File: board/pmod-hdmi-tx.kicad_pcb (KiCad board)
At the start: 2 copper layers, 42 x 43.2 mm, 35 parts, among them P1 PMOD-Device-x2-Type-XHS-Alt, U31 XC9140, U32 REG710-DBV

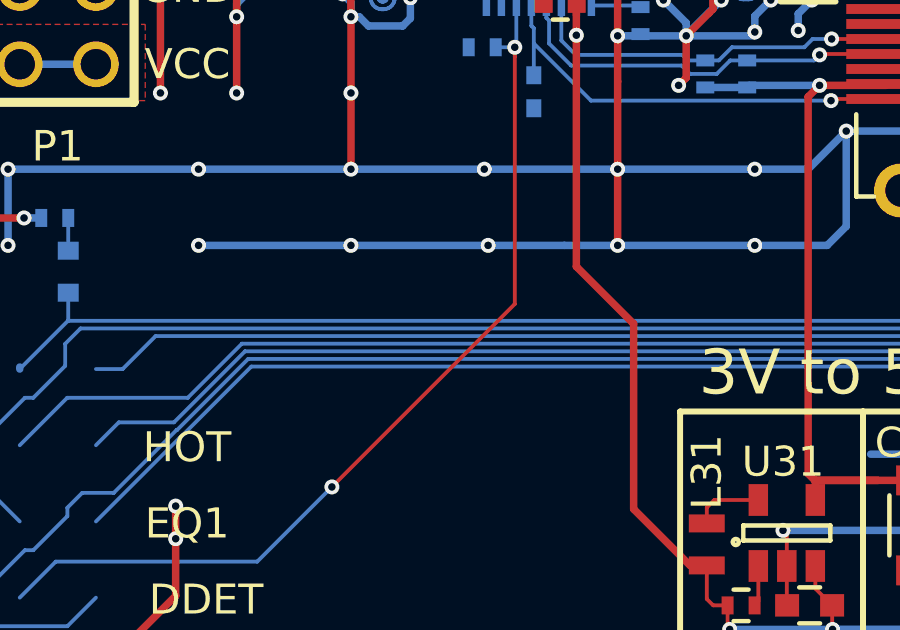
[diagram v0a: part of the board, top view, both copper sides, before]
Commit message: Fiddling with the silkscreen.
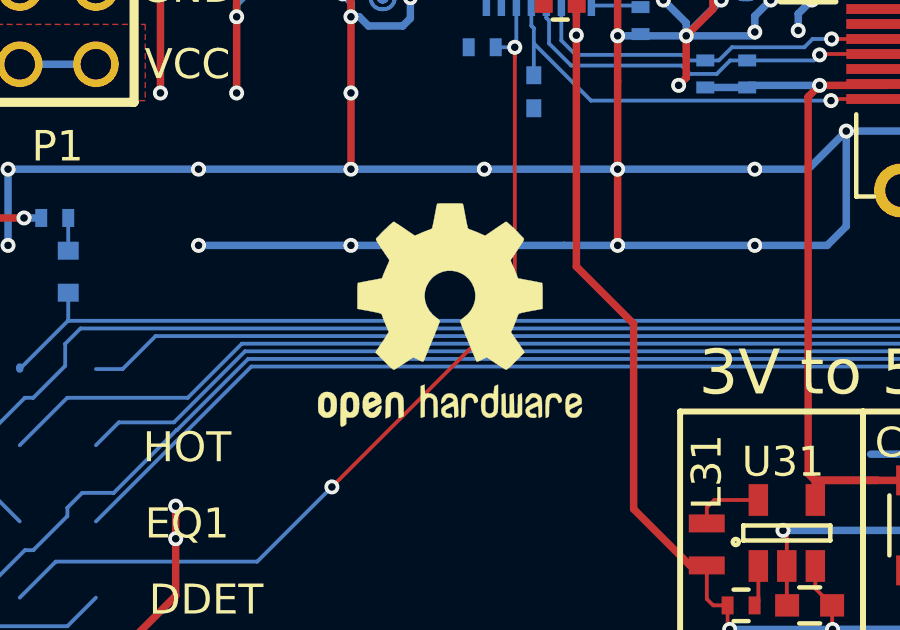
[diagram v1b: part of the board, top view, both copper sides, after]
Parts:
- added REF***: OSHW-Logo2_9.8x8mm_SilkScreen, Symbols:OSHW-Logo2_9.8x8mm_SilkScreen, F.Cu at (98.6, 95.0)
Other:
- board text added: "pmod-hdmi-tx ptn3363"
- board text added: "v0.0"

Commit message: Tweaking embedded version.
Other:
- board text added: "$Id$"
- board text added: "tx0.0"
- board text removed: "v0.0"
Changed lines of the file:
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@@
 (kicad_pcb (version 4) (host pcbnew 4.0.4+e1-6308~48~ubuntu14.04.1-stable)
   (general
-    (links 0)
+    (links 102)
     (no_connects 0)
     (area 48.857144 45.285715 236.214292 120.05)
     (thickness 1.6)
-    (drawings 128)
+    (drawings 129)
     (tracks 1763)
     (zones 0)
@@
       (xy -0.017575 -3.712307) (xy 0 -3.712308) (xy 0.139878 -3.712224)) (layer F.SilkS) (width 0.01))
   )
-  (gr_text v0.0 (at 121.0818 105.156) (layer B.SilkS)
+  (gr_text $Id$ (at 121.1072 109.2454) (layer B.SilkS)
     (effects (font (size 2.159 2.159) (thickness 0.53975)) (justify left mirror))
   )
+  (gr_text tx0.0 (at 121.0818 105.156) (layer B.SilkS)
+    (effects (font (size 2.159 2.159) (thickness 0.53975)) (justify left mirror))
+  )

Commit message: Tweaking a track.
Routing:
- net VCC3V3: track 106.6 -> 107.2 mm
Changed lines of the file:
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@@
     (thickness 1.6)
     (drawings 129)
-    (tracks 1763)
+    (tracks 1764)
     (zones 0)
     (modules 37)
@@
   (via (at 103.8352 75.0062) (size 0.5) (drill 0.25) (layers F.Cu B.Cu) (net 0))
   (via (at 103.8352 79.9846) (size 0.5) (drill 0.25) (layers F.Cu B.Cu) (net 0))
+  (segment (start 107.315 109.22) (end 106.6546 108.5596) (width 0.25) (layer F.Cu) (net 1))
+  (segment (start 106.6546 108.5596) (end 87.7224 108.5596) (width 0.25) (layer F.Cu) (net 1))
+  (segment (start 87.7224 108.5596) (end 86.75 109.532) (width 0.25) (layer F.Cu) (net 1))
   (segment (start 99.187 79.883) (end 99.187 79.502) (width 0.25) (layer F.Cu) (net 1))
   (segment (start 99.187 79.502) (end 98.7044 79.0194) (width 0.25) (layer F.Cu) (net 1))
@@
   (segment (start 104.6734 101.4984) (end 104.6734 95.3262) (width 0.25) (layer F.Cu) (net 1))
   (segment (start 107.1118 103.37864) (end 106.55364 103.37864) (width 0.25) (layer F.Cu) (net 1))
-  (segment (start 107.315 109.22) (end 87.062 109.22) (width 0.25) (layer F.Cu) (net 1))
-  (segment (start 87.062 109.22) (end 86.75 109.532) (width 0.25) (layer F.Cu) (net 1))
   (segment (start 110.49 109.22) (end 107.315 109.22) (width 0.25) (layer F.Cu) (net 1))
   (segment (start 111.3028 108.4072) (end 110.49 109.22) (width 0.25) (layer F.Cu) (net 1))

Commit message: Adding GND/VCC open area.
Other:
- board text added: "647f4a6"
- board text added: "VCC3V3"
- board text added: "tx0.1"
- board text removed: "$Id$"
- board text removed: "tx0.0"
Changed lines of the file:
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@@
-(kicad_pcb (version 4) (host pcbnew 4.0.4+e1-6308~48~ubuntu14.04.1-stable)
+(kicad_pcb (version 4) (host pcbnew 4.0.6-e0-6349~53~ubuntu14.04.1)
   (general
     (links 102)
@@
     (area 48.857144 45.285715 236.214292 120.05)
     (thickness 1.6)
-    (drawings 129)
+    (drawings 131)
     (tracks 1764)
     (zones 0)
@@
     (36 B.SilkS user)
     (37 F.SilkS user)
-    (38 B.Mask user hide)
-    (39 F.Mask user hide)
-    (40 Dwgs.User user hide)
+    (38 B.Mask user)
+    (39 F.Mask user)
+    (40 Dwgs.User user)
     (41 Cmts.User user hide)
     (42 Eco1.User user hide)
@@
       (xy -0.017575 -3.712307) (xy 0 -3.712308) (xy 0.139878 -3.712224)) (layer F.SilkS) (width 0.01))
   )
-  (gr_text $Id$ (at 121.1072 109.2454) (layer B.SilkS)
+  (gr_text GND (at 100.3935 107.6325) (layer B.SilkS)
+    (effects (font (size 1.5 1.5) (thickness 0.3)) (justify mirror))
+  )
+  (gr_text VCC3V3 (at 96.8375 107.7595) (layer F.SilkS)
+    (effects (font (size 1.5 1.5) (thickness 0.3)))
+  )
+  (gr_text 647f4a6 (at 121.1072 109.2454) (layer B.SilkS)
     (effects (font (size 2.159 2.159) (thickness 0.53975)) (justify left mirror))
   )
-  (gr_text tx0.0 (at 121.0818 105.156) (layer B.SilkS)
+  (gr_text tx0.1 (at 121.0818 105.156) (layer B.SilkS)
     (effects (font (size 2.159 2.159) (thickness 0.53975)) (justify left mirror))
   )
@@
       )
     )
+  )
+  (zone (net 0) (net_name "") (layer F.Mask) (hatch edge 0.508)
+    (connect_pads (clearance 0.2))
+    (min_thickness 0.254)
+    (fill yes (arc_segments 16) (thermal_gap 0.508) (thermal_bridge_width 0.508))
+    (polygon
+      (pts
+        (xy 92.453982 108.7755) (xy 97.279982 108.7755) (xy 97.279982 113.3475) (xy 92.453982 113.3475)
+      )
+    )
+  )
+  (zone (net 0) (net_name "") (layer B.Mask) (hatch edge 0.508)
+    (connect_pads (clearance 0.2))
+    (min_thickness 0.254)
+    (fill yes (arc_segments 16) (thermal_gap 0.508) (thermal_bridge_width 0.508))
+    (polygon
+      (pts
+        (xy 97.8535 108.7755) (xy 102.6795 108.7755) (xy 102.6795 113.3475) (xy 97.8535 113.3475)
+      )
+    )

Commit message: Fiddling with the silkscreen more.
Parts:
- moved REF*** 6.66 mm to (100.2, 101.5)
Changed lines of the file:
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@@
     (descr "QMOD Pin Header 2 x 6 pins")
     (tags CONN)
-    (fp_text reference PTX0 (at -0.762 -8.636) (layer F.SilkS)
+    (fp_text reference PTX0 (at -0.898 8.7685) (layer F.SilkS)
       (effects (font (size 1.016 1.016) (thickness 0.254)))
     )
@@
   )
   (module Symbols:OSHW-Logo2_9.8x8mm_SilkScreen (layer F.Cu)
-    (at 98.552 95.0214)
+    (at 100.203 101.473)
     (descr "Open Source Hardware Symbol")
     (tags "Logo Symbol OSHW")
@@
   (gr_line (start 80 113.342) (end 59 113.342) (layer Eco1.User) (width 0.2))
   (gr_line (start 79.5 70.162) (end 59 70.162) (layer Eco1.User) (width 0.2))
-  (gr_text "Low Speed & Control Signals" (at 97.663 111.887) (layer F.SilkS)
-    (effects (font (size 1.5 1.5) (thickness 0.3)))
-  )
-  (gr_text "High Speed" (at 86.995 71.247) (layer F.SilkS)
-    (effects (font (size 1.5 1.5) (thickness 0.3)))
-  )
+  (gr_text "Low Speed & Control Signals" (at 99.441 94.0435) (layer F.SilkS)
+    (effects (font (size 1.5 1.5) (thickness 0.3)))
+  )
+  (gr_text "High Speed" (at 89.0905 71.501) (layer F.SilkS)
+    (effects (font (size 1.5 1.5) (thickness 0.3)))
+  )

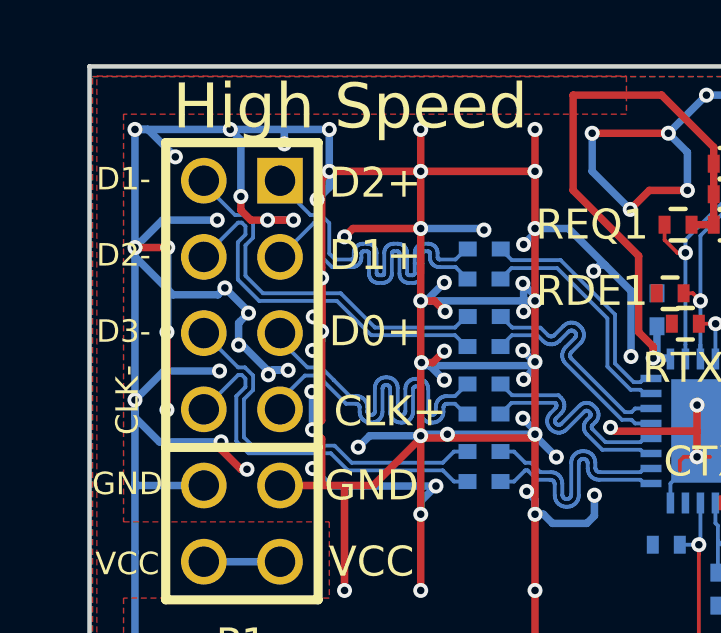
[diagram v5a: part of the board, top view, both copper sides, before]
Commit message: Fixing the high speed labels.
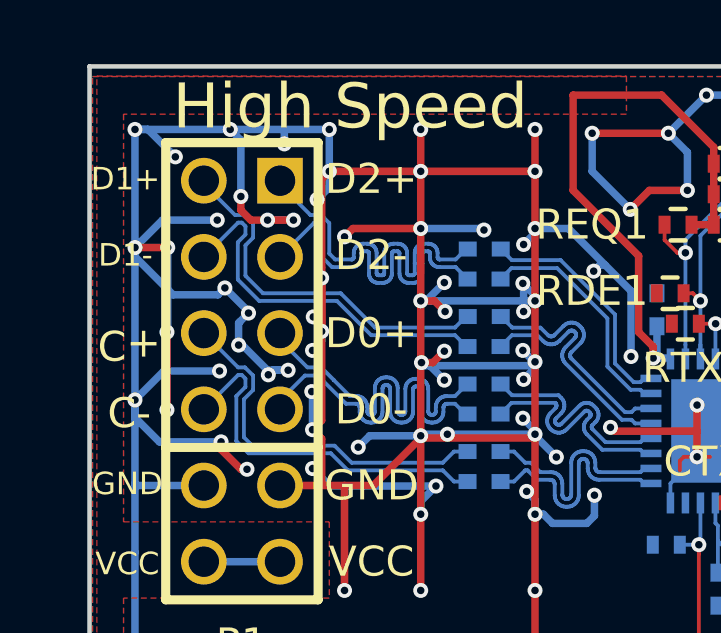
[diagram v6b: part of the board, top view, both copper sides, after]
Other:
- board text added: "C+"
- board text added: "C-"
- board text removed: "CLK+"
- board text removed: "CLK-"
- board text removed: "D3-"
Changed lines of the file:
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@@
   (page A4)
   (layers
-    (0 F.Cu signal)
-    (31 B.Cu signal)
+    (0 F.Cu signal hide)
+    (31 B.Cu signal hide)
     (32 B.Adhes user hide)
     (33 F.Adhes user hide)
@@
     (36 B.SilkS user)
     (37 F.SilkS user)
-    (38 B.Mask user)
-    (39 F.Mask user)
+    (38 B.Mask user hide)
+    (39 F.Mask user hide)
     (40 Dwgs.User user)
     (41 Cmts.User user hide)
@@
       (effects (font (size 1 1) (thickness 0.15)))
     )
-    (fp_text user D2+ (at 4.436 -6.281) (layer F.SilkS)
+    (fp_text user D2+ (at 4.309 -6.408) (layer F.SilkS)
       (effects (font (size 1 1) (thickness 0.15)))
     )
@@
       (xy -0.017575 -3.712307) (xy 0 -3.712308) (xy 0.139878 -3.712224)) (layer F.SilkS) (width 0.01))
   )
+  (gr_text C+ (at 81.7245 79.4385 180) (layer F.SilkS)
+    (effects (font (size 1 1) (thickness 0.15)) (justify mirror))
+  )
   (gr_text GND (at 100.3935 107.6325) (layer B.SilkS)
     (effects (font (size 1.5 1.5) (thickness 0.3)) (justify mirror))
@@
     (effects (font (size 1 1) (thickness 0.15)) (justify mirror))
   )
-  (gr_text CLK- (at 81.153 82.677 90) (layer B.SilkS)
+  (gr_text C- (at 81.7245 81.7245 360) (layer B.SilkS)
     (effects (font (size 1 1) (thickness 0.15)) (justify mirror))
   )
-  (gr_text D0- (at 82.042 79.629 90) (layer B.SilkS)
+  (gr_text C+ (at 81.7245 79.4385 360) (layer B.SilkS)
     (effects (font (size 1 1) (thickness 0.15)) (justify mirror))
   )
@@
     (effects (font (size 1 1) (thickness 0.15)) (justify mirror))
   )
-  (gr_text D2- (at 82.042 74.168 90) (layer B.SilkS)
+  (gr_text D1+ (at 82.042 74.168 90) (layer B.SilkS)
     (effects (font (size 1 1) (thickness 0.15)) (justify mirror))
   )
-  (gr_text CLK+ (at 89.916 81.28) (layer B.SilkS)
+  (gr_text D0- (at 89.789 81.5975) (layer B.SilkS)
     (effects (font (size 1 1) (thickness 0.15)) (justify mirror))
   )
-  (gr_text D0+ (at 89.916 78.74) (layer B.SilkS)
+  (gr_text D0+ (at 89.789 79.0575) (layer B.SilkS)
     (effects (font (size 1 1) (thickness 0.15)) (justify mirror))
   )
-  (gr_text D1+ (at 89.789 76.327) (layer B.SilkS)
+  (gr_text D2- (at 89.789 76.454) (layer B.SilkS)
     (effects (font (size 1 1) (thickness 0.15)) (justify mirror))
   )
@@
     (effects (font (size 0.75 0.75) (thickness 0.15)))
   )
-  (gr_text CLK- (at 81.661 81.28 90) (layer F.SilkS)
+  (gr_text C- (at 81.7245 81.7245 360) (layer F.SilkS)
+    (effects (font (size 1 1) (thickness 0.15)))
+  )
+  (gr_text D1- (at 81.5975 76.454) (layer F.SilkS)
     (effects (font (size 0.75 0.75) (thickness 0.15)))
   )
-  (gr_text D3- (at 81.534 78.994) (layer F.SilkS)
+  (gr_text D1+ (at 81.5975 73.914) (layer F.SilkS)
     (effects (font (size 0.75 0.75) (thickness 0.15)))
   )
-  (gr_text D2- (at 81.534 76.454) (layer F.SilkS)
-    (effects (font (size 0.75 0.75) (thickness 0.15)))
-  )
-  (gr_text D1- (at 81.534 73.914) (layer F.SilkS)
-    (effects (font (size 0.75 0.75) (thickness 0.15)))
-  )
-  (gr_text CLK+ (at 90.424 81.661) (layer F.SilkS)
+  (gr_text D0- (at 89.789 81.5975) (layer F.SilkS)
     (effects (font (size 1 1) (thickness 0.15)))
   )
-  (gr_text D0+ (at 89.916 78.994) (layer F.SilkS)
+  (gr_text D0+ (at 89.789 79.0575) (layer F.SilkS)
     (effects (font (size 1 1) (thickness 0.15)))
   )
-  (gr_text D1+ (at 89.916 76.454) (layer F.SilkS)
+  (gr_text D2- (at 89.789 76.454) (layer F.SilkS)
     (effects (font (size 1 1) (thickness 0.15)))
   )

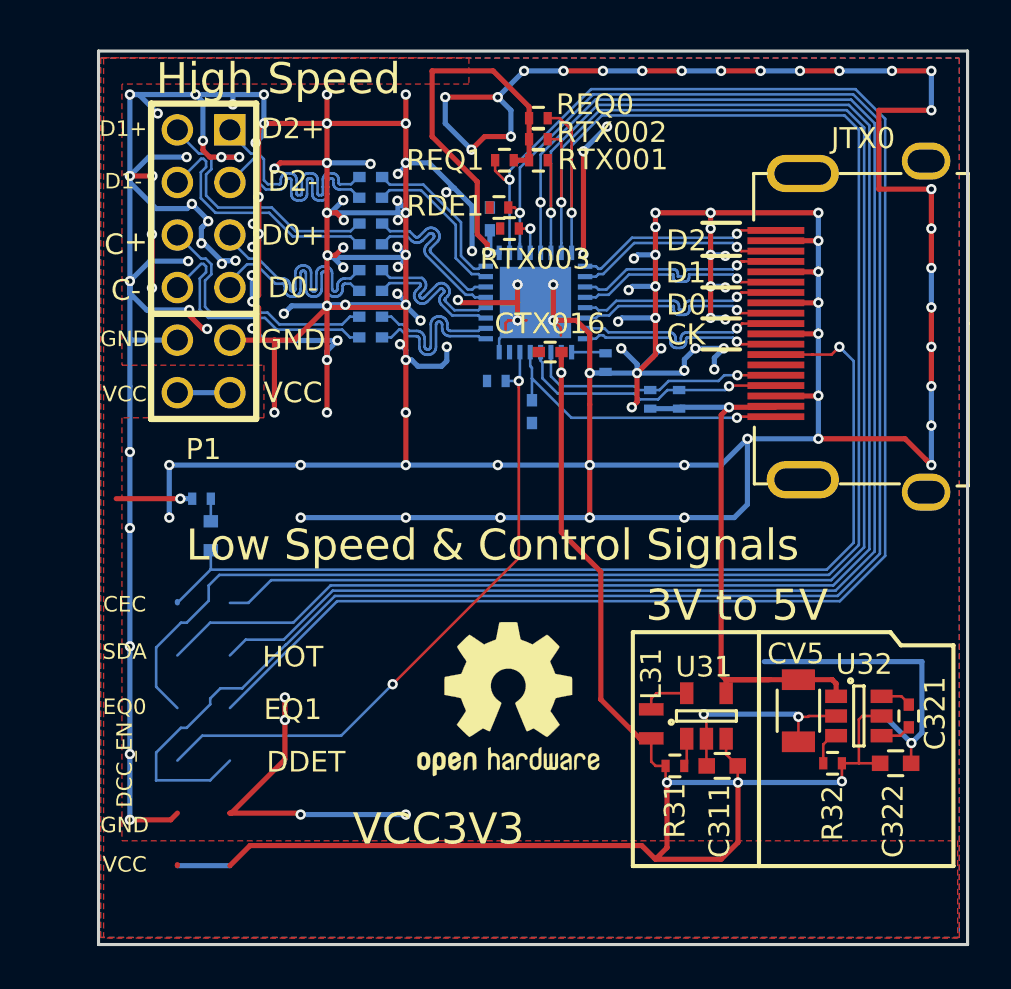
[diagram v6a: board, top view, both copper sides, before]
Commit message: Fixing the via sizes.
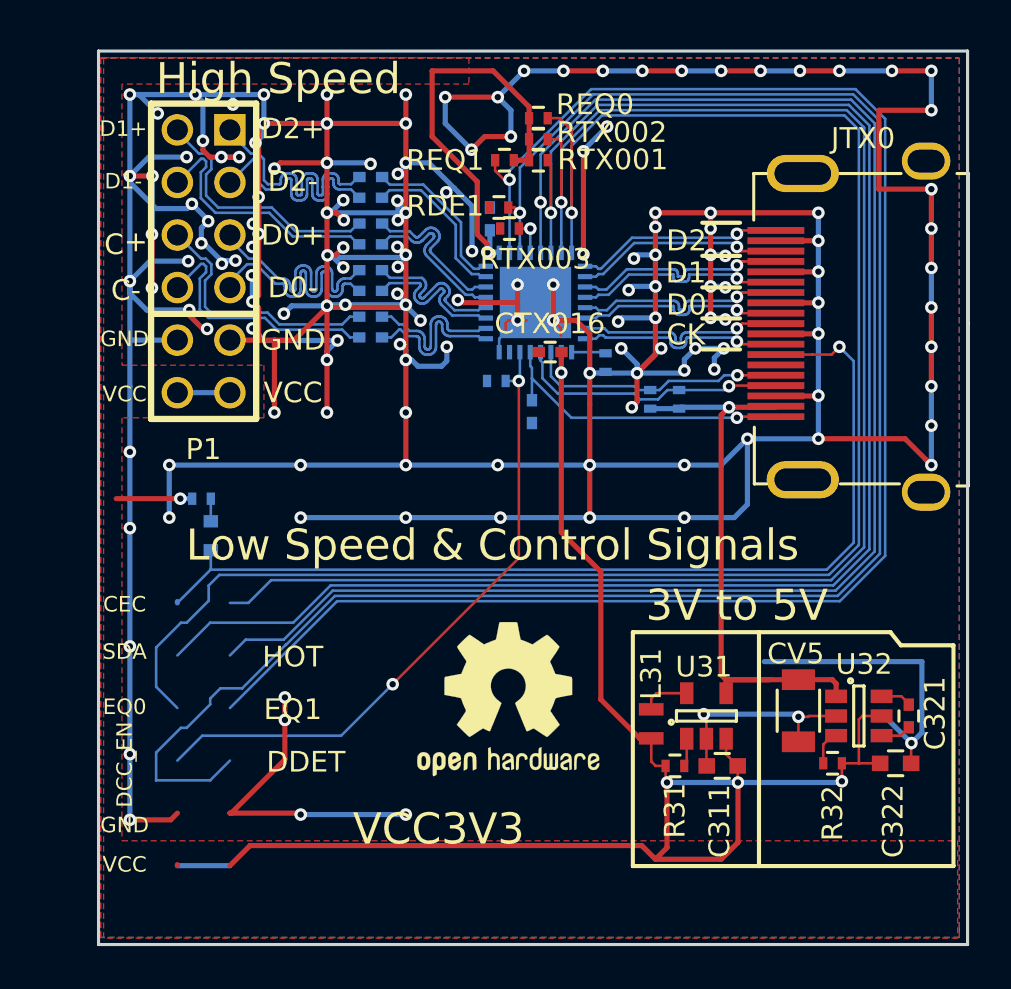
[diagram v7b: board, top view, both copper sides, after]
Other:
- net class Default: via_dia 0.5 -> 0.6096; via_drill 0.25 -> 0.3048
- net class HDMI_CAP2IC_DP0.0254/0.254: via_dia 0.5 -> 0.6096; via_drill 0.25 -> 0.3048
- net class HDMI_IC2PORT_DP0.0254/0.381: via_dia 0.5 -> 0.6096; via_drill 0.25 -> 0.3048
- net class HDMI_PMOD2CAP_DP0.0254/0.254: via_dia 0.5 -> 0.6096; via_drill 0.25 -> 0.3048
- net class PWR: via_dia 0.5 -> 0.6096; via_drill 0.25 -> 0.3048

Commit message: Setting clearance correctly.
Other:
- net class HDMI_CAP2IC_DP0.0254/0.254: clearance 0.126975 -> 0.127
- net class HDMI_IC2PORT_DP0.0254/0.381: clearance 0.126975 -> 0.127
- net class HDMI_PMOD2CAP_DP0.0254/0.254: clearance 0.126975 -> 0.127
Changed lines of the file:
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@@
-(kicad_pcb (version 4) (host pcbnew 4.0.6-e0-6349~53~ubuntu14.04.1)
+(kicad_pcb (version 4) (host pcbnew 4.0.4+e1-6308~48~ubuntu14.04.1-stable)
   (general
     (links 102)
@@
   (page A4)
   (layers
-    (0 F.Cu signal hide)
-    (31 B.Cu signal hide)
+    (0 F.Cu signal)
+    (31 B.Cu signal)
     (32 B.Adhes user hide)
     (33 F.Adhes user hide)
@@
   )
   (net_class HDMI_CAP2IC_DP0.0254/0.254 ""
-    (clearance 0.126975)
+    (clearance 0.127)
     (trace_width 0.127)
     (via_dia 0.6096)
@@
   )
   (net_class HDMI_IC2PORT_DP0.0254/0.381 ""
-    (clearance 0.126975)
+    (clearance 0.127)
     (trace_width 0.127)
     (via_dia 0.6096)
@@
   )
   (net_class HDMI_PMOD2CAP_DP0.0254/0.254 ""
-    (clearance 0.126975)
+    (clearance 0.127)
     (trace_width 0.127)
     (via_dia 0.6096)
@@
     (effects (font (size 1 1) (thickness 0.15)) (justify mirror))
   )
-  (gr_text C- (at 81.7245 81.7245 360) (layer B.SilkS)
+  (gr_text C- (at 81.7245 81.7245) (layer B.SilkS)
     (effects (font (size 1 1) (thickness 0.15)) (justify mirror))
   )
-  (gr_text C+ (at 81.7245 79.4385 360) (layer B.SilkS)
+  (gr_text C+ (at 81.7245 79.4385) (layer B.SilkS)
     (effects (font (size 1 1) (thickness 0.15)) (justify mirror))
   )
@@
     (effects (font (size 0.75 0.75) (thickness 0.15)))
   )
-  (gr_text C- (at 81.7245 81.7245 360) (layer F.SilkS)
+  (gr_text C- (at 81.7245 81.7245) (layer F.SilkS)
     (effects (font (size 1 1) (thickness 0.15)))
   )
